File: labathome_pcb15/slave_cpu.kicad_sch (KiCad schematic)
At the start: 49 parts, among them J1 HALL, J25 TC-2030, J26 PROG STM, J27 ADDA, J28 Brushless, J30 Srv3, J31 Srv0, J32 Srv1, J33 Srv2, J34 STM32 EXT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

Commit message: Various changes / bugfixes / refactorings
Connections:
- net BL_RESET: now also U5.56 (PB3); no longer U5.55 (PD2)
- new net LCD_RES: U5.55 (PD2)
- no-connect marks 3 -> 2
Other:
- note removed: "Overcurrent ca. 1,5A"
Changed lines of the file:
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@@
-	)
-	(no_connect
-		(at 68.58 87.63)
 	)
 	(no_connect
@@
 			)
 			(justify left bottom)
-		)
-	)
-	(text "Overcurrent ca. 1,5A"
-		(exclude_from_sim no)
-		(at 238.506 74.676 0)
-		(effects
-			(font
-				(size 1.27 1.27)
-			)
 		)
 	)
@@
 	(global_label "BL_RESET"
 		(shape output)
-		(at 33.02 54.61 180)
+		(at 68.58 87.63 0)
 		(fields_autoplaced yes)
 		(effects
@@
 				(size 1.27 1.27)
 			)
-			(justify right)
+			(justify left)
 		)
 		(property "Intersheetrefs" "${INTERSHEET_REFS}"
-			(at 21.024 54.61 0)
+			(at 80.576 87.63 0)
 			(effects
 				(font
 					(size 1.27 1.27)
 				)
-				(justify right)
+				(justify left)
 				(hide yes)
 			)
@@
 				(hide yes)
 			)
+		)
+	)
+	(global_label "LCD_RES"
+		(shape output)
+		(at 33.02 54.61 180)
+		(fields_autoplaced yes)
+		(effects
+			(font
+				(size 1.27 1.27)
+			)
+			(justify right)
+		)
+		(property "Intersheetrefs" "${INTERSHEET_REFS}"
+			(at 21.8706 54.61 0)
+			(effects
+				(font
+					(size 1.27 1.27)
+				)
+				(justify right)
+				(hide yes)
+			)

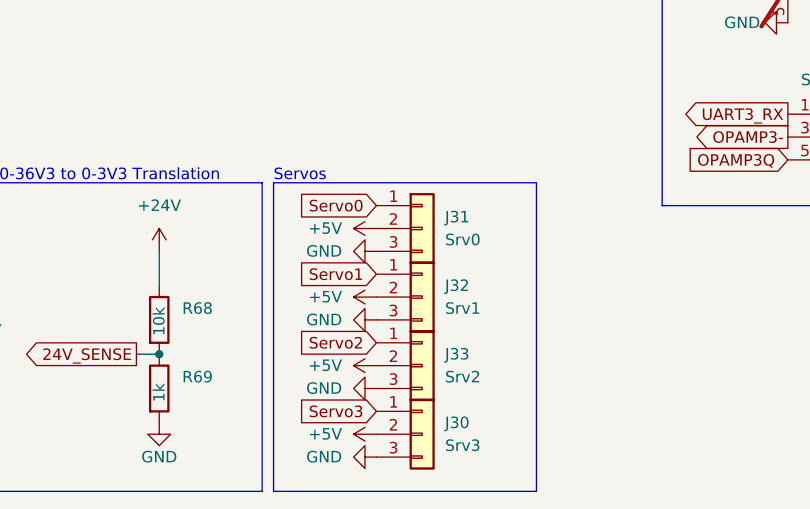
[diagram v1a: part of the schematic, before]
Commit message: ec11 smd, LCD Reset from ESP32 with jumper, six servos
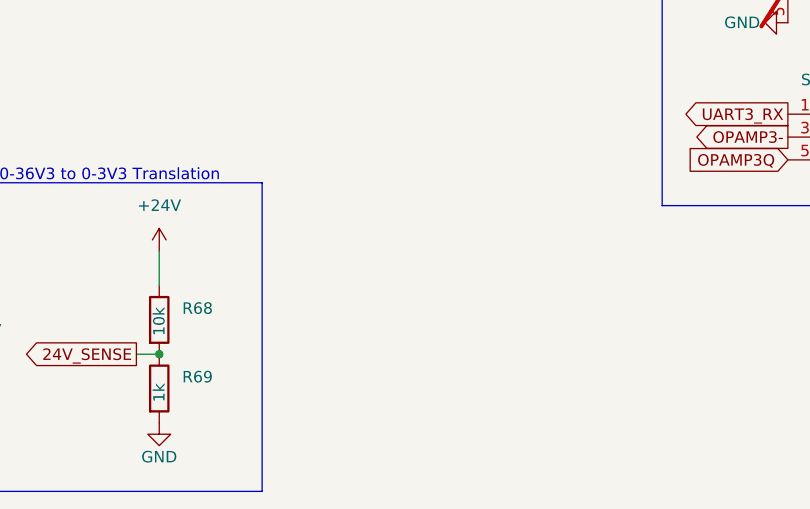
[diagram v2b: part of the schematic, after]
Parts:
- removed J30: Srv3, liebler_CONN:PinHeader_1x03_P2.54mm_Vertical_smallerCourtyard, symbol Connector_Generic:Conn_01x03
- removed J31: Srv0, liebler_CONN:PinHeader_1x03_P2.54mm_Vertical_smallerCourtyard, symbol Connector_Generic:Conn_01x03
- removed J32: Srv1, liebler_CONN:PinHeader_1x03_P2.54mm_Vertical_smallerCourtyard, symbol Connector_Generic:Conn_01x03
- removed J33: Srv2, liebler_CONN:PinHeader_1x03_P2.54mm_Vertical_smallerCourtyard, symbol Connector_Generic:Conn_01x03
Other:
- note removed: "Servos"

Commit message: Minimal changes
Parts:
- removed J26: PROG STM, liebler_CONN:PinHeader_2x03_P1.27mm_Vertical_SMD_handsolder, symbol Connector_Generic:Conn_02x03_Odd_Even
- removed TP1: RX, TestPoint:TestPoint_THTPad_D1.5mm_Drill0.7mm, symbol Connector:TestPoint_Small
- added J36: PROG_STM, Connector_PinSocket_2.54mm:PinSocket_2x06_P2.54mm_Vertical_SMD, symbol Connector_Generic:Conn_02x06_Odd_Even
- added JP4: 5V, Jumper:SolderJumper-2_P1.3mm_Open_RoundedPad1.0x1.5mm, symbol Jumper:SolderJumper_2_Open
- added JP5: 3V3, Jumper:SolderJumper-2_P1.3mm_Open_RoundedPad1.0x1.5mm, symbol Jumper:SolderJumper_2_Open
- added R65: 10k, Resistor_SMD:R_0201_0603Metric, symbol Device:R
- added R71: 1k, Resistor_SMD:R_0402_1005Metric, symbol Device:R
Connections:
- net +3V3: now also JP5.1 (A)
- net GND: now also J36.5 (Pin_5), J36.6 (Pin_6), R71.2
- net STM32_RESET: now also J36.2 (Pin_2)
- net SWCLK: now also J36.8 (Pin_8)
- net SWDIO: now also J36.10 (Pin_10)
- net UART4_RX: now also J36.9 (Pin_9)
- net UART4_TX: now also J36.7 (Pin_7)
- net 24V_INPUT: now reaches U5.58 (PB5)
- net 24V_INPUT: now also R65.2, R71.1
- new net: J36.11 (Pin_11), J36.12 (Pin_12), JP5.2 (B)
- new net: J36.3 (Pin_3), J36.4 (Pin_4), JP4.1 (A)
- new net +5V: JP4.2 (B)
- new net 24V_INP: J36.1 (Pin_1), R65.1
- no-connect marks 2 -> 1

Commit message: IP5306
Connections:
- net FAN_DRIVE: now also U5.17 (PA3); no longer U5.14 (PA2)
- net LED_WHITE_P: now also U5.14 (PA2); no longer U5.17 (PA3)
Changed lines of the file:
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@@
 	(global_label "FAN_DRIVE"
 		(shape output)
-		(at 68.58 41.91 0)
+		(at 68.58 44.45 0)
 		(fields_autoplaced yes)
 		(effects
@@
 		)
 		(property "Intersheetrefs" "${INTERSHEET_REFS}"
-			(at 81.4229 41.91 0)
+			(at 81.4229 44.45 0)
 			(effects
 				(font
@@
 	(global_label "LED_WHITE_P"
 		(shape output)
-		(at 68.58 44.45 0)
+		(at 68.58 41.91 0)
 		(fields_autoplaced yes)
 		(effects
@@
 		)
 		(property "Intersheetrefs" "${INTERSHEET_REFS}"
-			(at 83.7208 44.45 0)
+			(at 83.7208 41.91 0)
 			(effects
 				(font

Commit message: bsec
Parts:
- C39: footprint Capacitor_THT:CP_Radial_D6.3mm_P2.50mm -> Capacitor_SMD:CP_Elec_6.3x5.4
- R38: footprint Resistor_THT:R_Axial_DIN0309_L9.0mm_D3.2mm_P12.70mm_Horizontal -> Resistor_SMD:R_2512_6332Metric
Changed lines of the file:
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@@
 			)
 		)
-		(property "Footprint" "Resistor_THT:R_Axial_DIN0309_L9.0mm_D3.2mm_P12.70mm_Horizontal"
+		(property "Footprint" "Resistor_SMD:R_2512_6332Metric"
 			(at 248.412 59.69 90)
 			(effects
@@
 			)
 		)
-		(property "Footprint" "Capacitor_THT:CP_Radial_D6.3mm_P2.50mm"
+		(property "Footprint" "Capacitor_SMD:CP_Elec_6.3x5.4"
 			(at 263.8552 66.04 0)
 			(effects

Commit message: Added stepper, no DRC errors, not yet optimized
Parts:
- R38: footprint Resistor_SMD:R_2512_6332Metric -> Resistor_SMD:R_2010_5025Metric
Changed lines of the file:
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@@
 			)
 		)
-		(property "Footprint" "Resistor_SMD:R_2512_6332Metric"
+		(property "Footprint" "Resistor_SMD:R_2010_5025Metric"
 			(at 248.412 59.69 90)
 			(effects

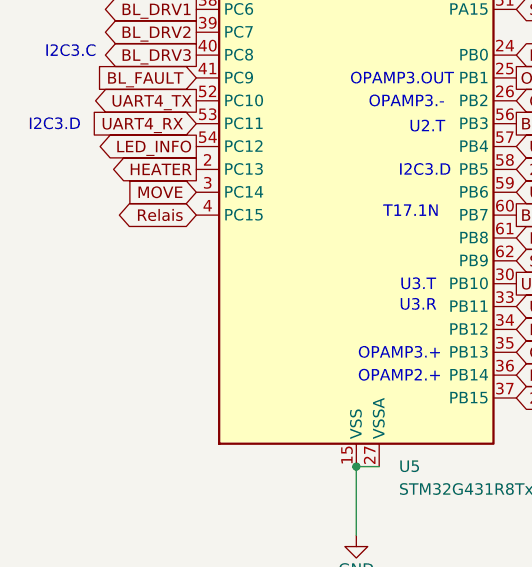
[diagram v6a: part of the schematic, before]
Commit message: Layout improvement; use common enable signal for steppers
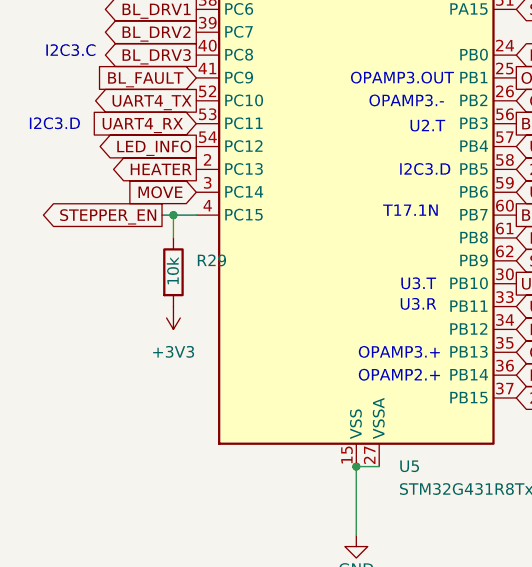
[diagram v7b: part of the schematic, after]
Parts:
- added R29: 10k, Resistor_SMD:R_0201_0603Metric, symbol Device:R
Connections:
- net +3V3: now also R29.2
- net Relais renamed STEPPER_EN
- net STEPPER_EN: now also R29.1
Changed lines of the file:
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@@
 	)
 	(junction
+		(at 30.48 97.79)
+		(diameter 0)
+		(color 0 0 0 0)
+	)
+	(junction
 		(at 250.19 66.04)
 		(diameter 0)
@@
 	(wire
 		(pts
+			(xy 29.21 97.79) (xy 30.48 97.79)
+		)
+		(stroke
+			(width 0)
+			(type default)
+		)
+	)
+	(wire
+		(pts
 			(xy 59.69 22.86) (xy 64.77 22.86)
 		)
@@
 	(wire
 		(pts
+			(xy 30.48 97.79) (xy 30.48 100.33)
+		)
+		(stroke
+			(width 0)
+			(type default)
+		)
+	)
+	(wire
+		(pts
 			(xy 55.88 20.32) (xy 55.88 15.24)
 		)
@@
 	(wire
 		(pts
+			(xy 30.48 97.79) (xy 33.02 97.79)
+		)
+		(stroke
+			(width 0)
+			(type default)
+		)
+	)
+	(wire
+		(pts
 			(xy 49.53 181.61) (xy 49.53 179.07)
 		)
@@
 		)
 	)
+	(global_label "STEPPER_EN"
+		(shape output)
+		(at 29.21 97.79 180)
+		(fields_autoplaced yes)
+		(effects
+			(font
+				(size 1.27 1.27)
+			)
+			(justify right)
+		)
+		(property "Intersheetrefs" "${INTERSHEET_REFS}"
+			(at 14.4926 97.79 0)
+			(effects
+				(font
+					(size 1.27 1.27)
+				)
+				(justify right)
+				(hide yes)
+			)
+		)
+	)
 	(global_label "BL_DRV3"
 		(shape input)
@@
 		)
 	)
-	(global_label "Relais"
-		(shape bidirectional)
-		(at 33.02 97.79 180)
-		(fields_autoplaced yes)
-		(effects
-			(font
-				(size 1.27 1.27)
-			)
-			(justify right)
-		)
-		(property "Intersheetrefs" "${INTERSHEET_REFS}"
-			(at 23.1178 97.79 0)
-			(effects
-				(font
-					(size 1.27 1.27)
-				)
-				(justify right)
-				(hide yes)
-			)
-		)
-	)
 	(global_label "BL_HALL2"
 		(shape output)
@@
 	)
 	(symbol
+		(lib_id "Device:R")
+		(at 30.48 104.14 0)
+		(unit 1)
+		(exclude_from_sim no)
+		(in_bom yes)
+		(on_board yes)
+		(dnp no)
+		(property "Reference" "R29"
+			(at 33.02 102.8699 0)
+			(effects
+				(font
+					(size 1.27 1.27)
+				)
+				(justify left)
+			)
+		)
+		(property "Value" "10k"
+			(at 30.48 105.664 90)
+			(effects
+				(font
+					(size 1.27 1.27)
+				)
+				(justify left)
+			)
+		)
+		(property "Footprint" "Resistor_SMD:R_0201_0603Metric"
+			(at 28.702 104.14 90)
+			(effects
+				(font
+					(size 1.27 1.27)
+				)
+				(hide yes)
+			)
+		)
+		(property "Datasheet" "~"
+			(at 30.48 104.14 0)
+			(effects
+				(font
+					(size 1.27 1.27)
+				)
+				(hide yes)
+			)
+		)
+		(property "Description" "Resistor"
+			(at 30.48 104.14 0)
+			(effects
+				(font
+					(size 1.27 1.27)
+				)
+				(hide yes)
+			)
+		)
+		(pin "1"
+		)
+		(pin "2"
+		)
+		(instances
+			(project "labathome_pcb15"
+				(path "/e4d6926a-1a8b-424d-97c4-66b6ad87e4ac/88291a06-4a87-426a-8cf8-e855480a1e3f"
+					(reference "R29")
+					(unit 1)
+				)
+			)
+		)
+	)
+	(symbol
 		(lib_id "power:GND")
 		(at 34.29 189.23 0)
@@
 					(unit 1)
 				)
+			)
+		)
+	)
+	(symbol
+		(lib_id "power:+3V3")
+		(at 30.48 107.95 180)
+		(unit 1)
+		(exclude_from_sim no)
+		(in_bom yes)
+		(on_board yes)
+		(dnp no)
+		(fields_autoplaced yes)
+		(property "Reference" "#PWR035"
+			(at 30.48 104.14 0)
+			(effects
+				(font
+					(size 1.27 1.27)
+				)
+				(hide yes)
+			)
+		)
+		(property "Value" "+3V3"
+			(at 30.48 113.03 0)
+			(effects
+				(font
+					(size 1.27 1.27)
+				)
+			)
+		)
+		(property "Footprint" ""
+			(at 30.48 107.95 0)
+			(effects
+				(font
+					(size 1.27 1.27)
+				)
+				(hide yes)
+			)
+		)
+		(property "Datasheet" ""
+			(at 30.48 107.95 0)
+			(effects
+				(font
+					(size 1.27 1.27)
+				)
+				(hide yes)
+			)
+		)
+		(property "Description" "Power symbol creates a global label with name \"+3V3\""
+			(at 30.48 107.95 0)
+			(effects
+				(font
+					(size 1.27 1.27)
+				)
+				(hide yes)
+			)
+		)
+		(pin "1"
+		)
+		(instances
+			(project "labathome_pcb15"
+				(path "/e4d6926a-1a8b-424d-97c4-66b6ad87e4ac/88291a06-4a87-426a-8cf8-e855480a1e3f"
+					(reference "#PWR035")
+					(unit 1)
+				)
